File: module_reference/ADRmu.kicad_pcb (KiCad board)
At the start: 4 copper layers, 160 x 100 mm, 142 parts, among them J101 Harting 09042326831, J102 10Vf, J103 10Vs, J104 7Vref, J105 Lo, J301 Conn_01x01, J302 Conn_01x01, J303 Conn_01x01, J304 Conn_01x01, J305 Conn_01x01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

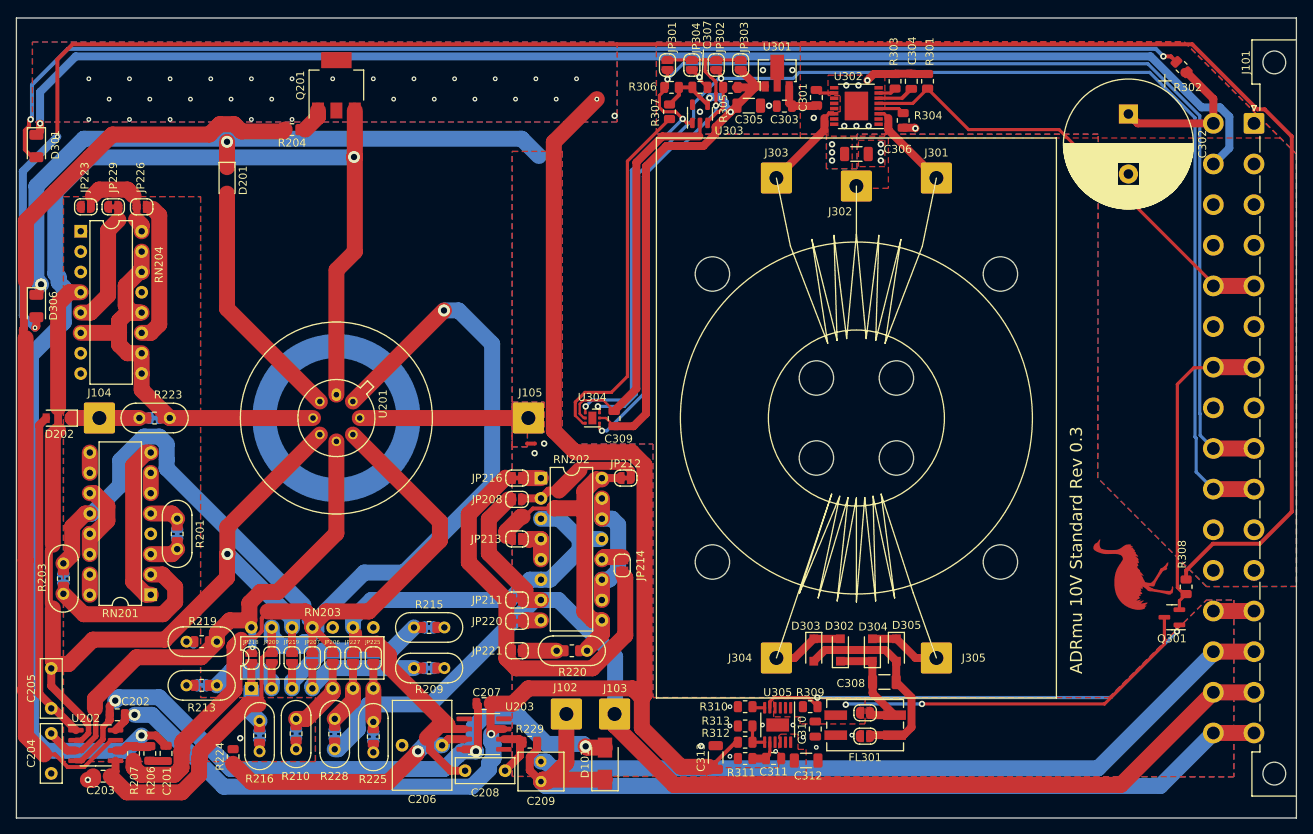
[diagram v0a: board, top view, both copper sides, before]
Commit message: switched to addressable eeprom
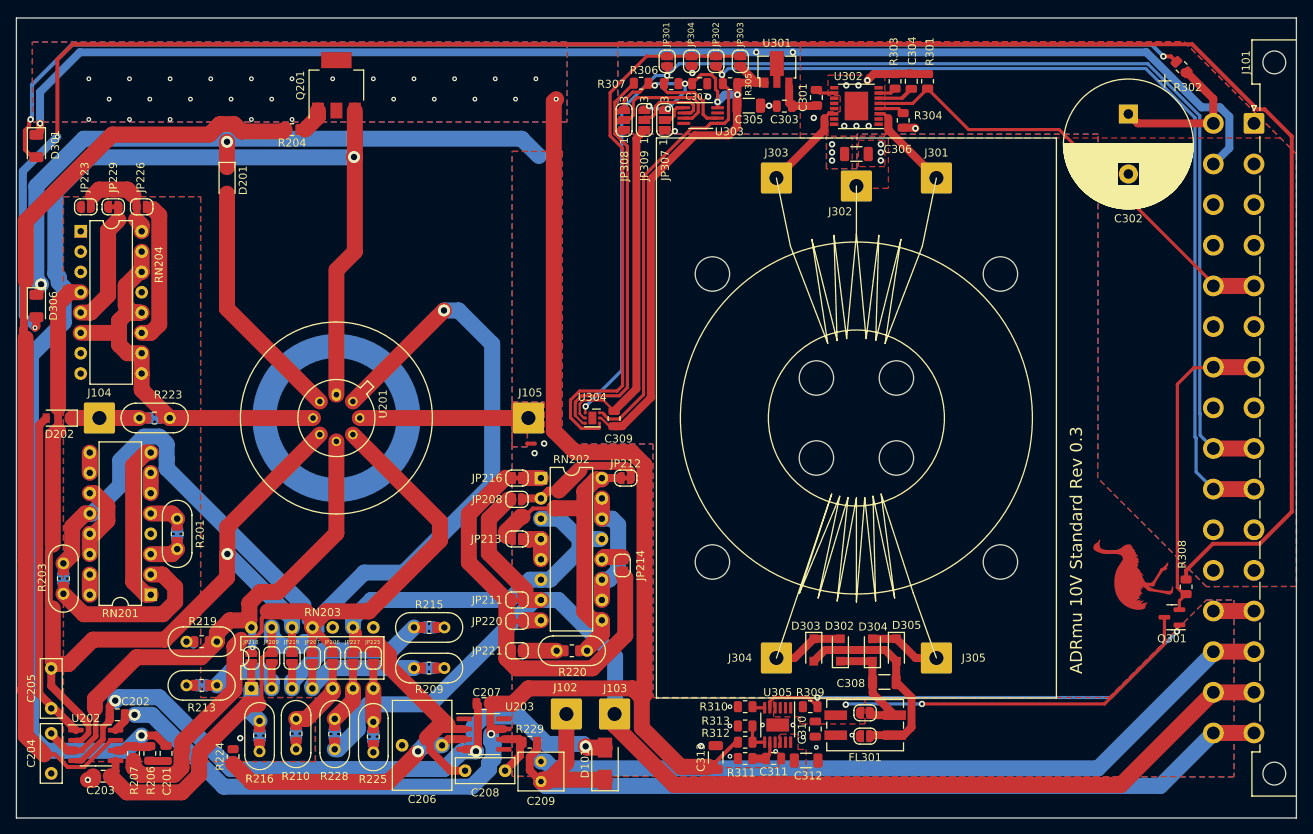
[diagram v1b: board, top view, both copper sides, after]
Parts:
- added JP307: Jumper_3_Open, Jumper:SolderJumper-3_P1.3mm_Open_RoundedPad1.0x1.5mm_NumberLabels, F.Cu at (151.0, 62.8)
- added JP308: Jumper_3_Open, Jumper:SolderJumper-3_P1.3mm_Open_RoundedPad1.0x1.5mm_NumberLabels, F.Cu at (146.0, 62.8)
- added JP309: Jumper_3_Open, Jumper:SolderJumper-3_P1.3mm_Open_RoundedPad1.0x1.5mm_NumberLabels, F.Cu at (148.5, 62.8)
- U303: value 24AA02-OT -> 24LC02; footprint Package_TO_SOT_SMD:SOT-23-5 -> Package_SO:MSOP-8_3x3mm_P0.65mm
- moved R307 5.03 mm to (148.1, 58.2), turned to 180 degrees
- moved JP301 0.47 mm to (151.3, 55.4)
- moved JP302 0.47 mm to (157.4, 55.4)
- moved JP303 0.47 mm to (160.5, 55.4)
- moved JP304 0.47 mm to (154.4, 55.4)
- moved C307 0.47 mm to (155.4, 58.2)
- moved R305 0.47 mm to (159.2, 58.2)
- moved R306 0.47 mm to (151.9, 58.2)
- moved U301 0.47 mm to (165.1, 56.4)
- moved U303 0.24 mm to (155.5, 62.2), turned to 0 degrees
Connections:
- U303 pad 1: /DC-DC/SCL -> /DC-DC/U303_a0
- U303 pad 2: GND -> /DC-DC/U303_a1
- U303 pad 3: /DC-DC/SDA -> /DC-DC/U303_a2
- U303 pad 4: +3V3 -> GND
- U303 pad 5: unconnected-(U303-Pad5) -> /DC-DC/SDA
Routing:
- net +3V3: track 73.4 -> 89.2 mm, vias 2 -> 6
- net /DC-DC/U303_a2: track 0.00 -> 15.0 mm
- net /DC-DC/U303_a1: track 0.00 -> 9.88 mm
- net GND: track 231.0 -> 224.0 mm, vias 16 -> 17
- net /DC-DC/U304_add0: track 64.0 -> 69.7 mm, vias 2 -> 0
- net /DC-DC/SCL: track 171.5 -> 176.7 mm, vias 3 -> 2
- net /DC-DC/U304_alert: track 45.5 -> 50.3 mm
- net /DC-DC/U303_a0: track 0.00 -> 3.40 mm
- net /DC-DC/SDA: track 172.3 -> 169.9 mm, vias 2 -> 1
- net /DC-DC/12Vf: track 188.0 -> 185.9 mm, vias 32 -> 29

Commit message: I shall waste not a copper
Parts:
- moved U304 3.35 mm to (144.5, 97.8)
- moved C309 3.35 mm to (147.2, 97.9)
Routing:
- net /DC-DC/U304_add0: track 69.7 -> 64.7 mm
- net /DC-DC/U304_alert: track 50.3 -> 45.3 mm
- net +3V3: track 89.2 -> 85.4 mm
- net /DC-DC/SDA: track 169.9 -> 166.4 mm
- net GNDA: track 177.8 -> 174.8 mm
- net /ref/ADR_Pin8: track 121.2 -> 118.6 mm
- net GND: track 224.0 -> 221.9 mm
- net /DC-DC/SCL: track 176.7 -> 174.6 mm
- net /ref/7Vref: track 13.3 -> 12.3 mm
- net /ref/U202B_out: track 116.1 -> 115.5 mm
- added copper zone on B.Cu, net /ref/10Vsense
- added copper zone on F.Cu, net /ref/ADR_Pin3
- added copper zone on B.Cu, net /ref/ADR_Pin4
- added copper zone on F.Cu, net /ref/ADR_Pin4
- added copper zone on F.Cu, net /ref/ADR_Pin6
- added copper zone on B.Cu, net /ref/ADR_Pin8
- added copper zone on F.Cu, net /ref/ADR_Pin8
- added copper zone on F.Cu, net /ref/RN202_Pin16
- added copper zone on F.Cu, net /ref/U203_-in
- added copper zone on B.Cu, net /ref/heater+
- added copper zone on F.Cu, net /ref/heater-

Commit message: asdf
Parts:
- moved D301 1.12 mm to (71.4, 66.0)
- moved D306 1.12 mm to (71.4, 86.0)
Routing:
- net /DC-DC/pwr_LED: track 155.8 -> 158.5 mm

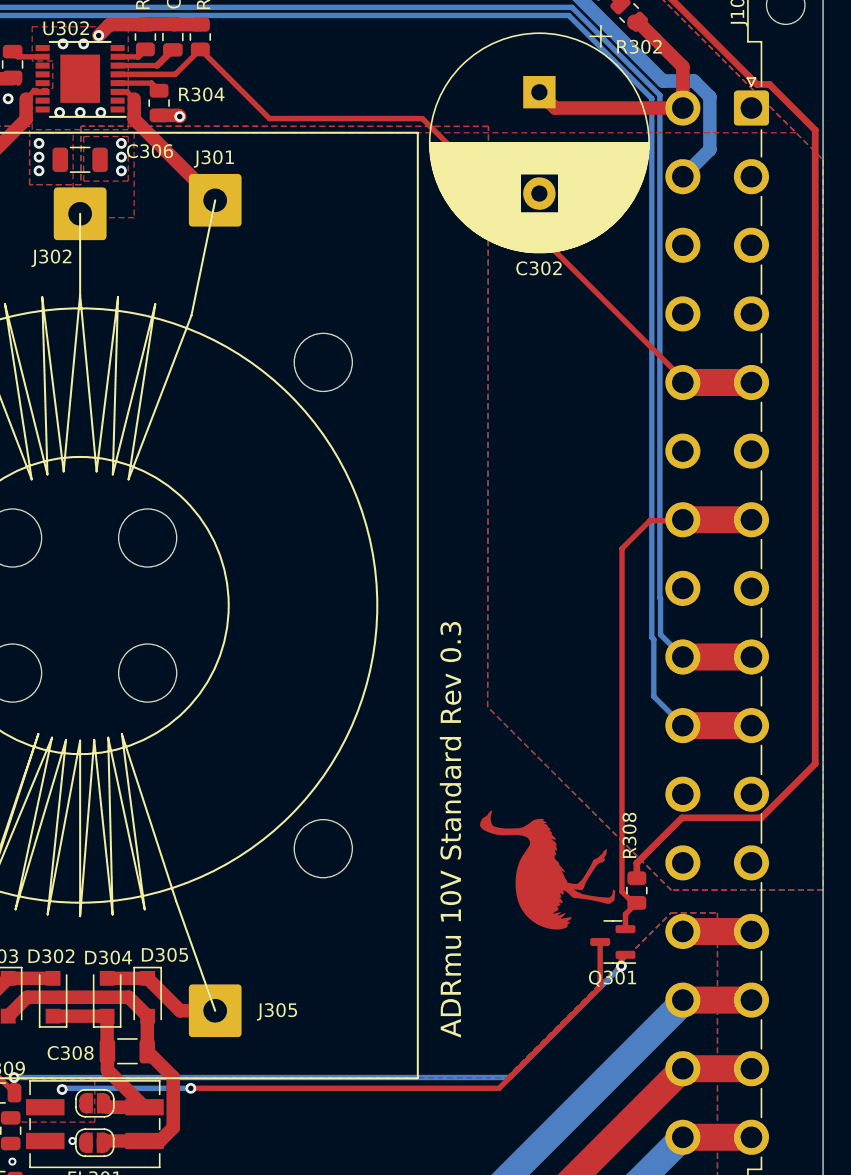
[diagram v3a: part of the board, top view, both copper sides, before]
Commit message: backplane connector changes
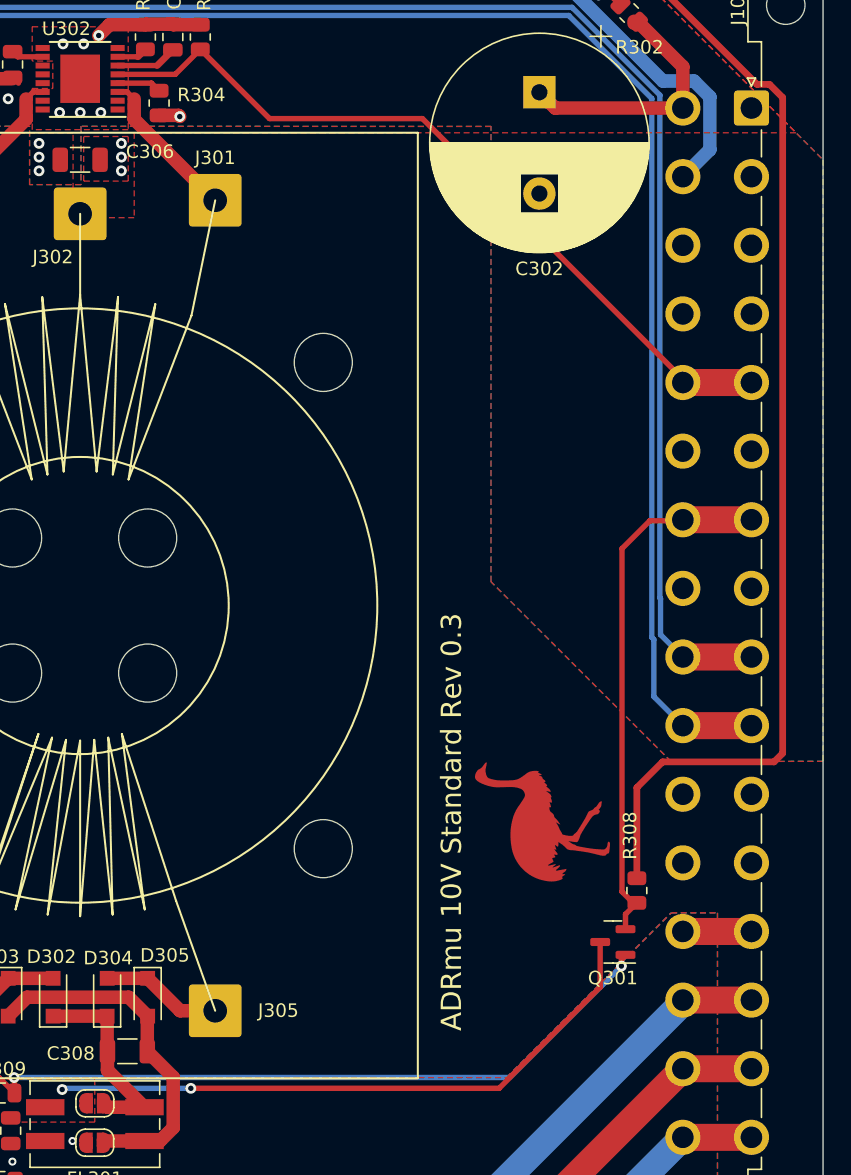
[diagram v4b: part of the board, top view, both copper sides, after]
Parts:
- moved SYM101 3.58 mm to (209.2, 116.0)
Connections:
- J101 pad a22: GND -> unconnected-(J101-Pada22)
- J101 pad a24: GND -> unconnected-(J101-Pada24)
- J101 pad c22: GND -> unconnected-(J101-Padc22)
- J101 pad c24: GND -> unconnected-(J101-Padc24)
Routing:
- net /DC-DC/status_LED: track 261.2 -> 260.6 mm
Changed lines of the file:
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@@
       (disableapertmacros false)
       (usegerberextensions false)
-      (usegerberattributes true)
+      (usegerberattributes false)
       (usegerberadvancedattributes true)
       (creategerberjobfile true)
@@
   (net 80 "/DC-DC/U303_a2")
   (net 81 "/DC-DC/U303_a1")
+  (net 82 "unconnected-(J101-Pada22)")
+  (net 83 "unconnected-(J101-Pada24)")
+  (net 84 "unconnected-(J101-Padc22)")
+  (net 85 "unconnected-(J101-Padc24)")
   (footprint "Resistor_SMD:R_0805_2012Metric" (layer "F.Cu")
     (at 151.8514 58.2096 180)
@@
       (net 6 "/DC-DC/SDA") (pinfunction "Pin_a20") (pintype "passive"))
     (pad "a22" thru_hole circle locked (at 53.34 0 270) (size 2.6 2.6) (drill 1.6) (layers *.Cu *.Mask)
-      (net 2 "GND") (pinfunction "Pin_a22") (pintype "passive"))
+      (net 82 "unconnected-(J101-Pada22)") (pinfunction "Pin_a22") (pintype "passive+no_connect"))
     (pad "a24" thru_hole circle locked (at 58.42 0 270) (size 2.6 2.6) (drill 1.6) (layers *.Cu *.Mask)
-      (net 2 "GND") (pinfunction "Pin_a24") (pintype "passive"))
+      (net 83 "unconnected-(J101-Pada24)") (pinfunction "Pin_a24") (pintype "passive+no_connect"))
     (pad "a26" thru_hole circle locked (at 63.5 0 270) (size 2.6 2.6) (drill 1.6) (layers *.Cu *.Mask)
       (net 76 "GNDA") (pinfunction "Pin_a26") (pintype "passive"))
@@
       (net 6 "/DC-DC/SDA") (pinfunction "Pin_c20") (pintype "passive"))
     (pad "c22" thru_hole circle locked (at 53.34 5.08 270) (size 2.6 2.6) (drill 1.6) (layers *.Cu *.Mask)
-      (net 2 "GND") (pinfunction "Pin_c22") (pintype "passive"))
+      (net 84 "unconnected-(J101-Padc22)") (pinfunction "Pin_c22") (pintype "passive+no_connect"))
     (pad "c24" thru_hole circle locked (at 58.42 5.08 270) (size 2.6 2.6) (drill 1.6) (layers *.Cu *.Mask)
-      (net 2 "GND") (pinfunction "Pin_c24") (pintype "passive"))
+      (net 85 "unconnected-(J101-Padc24)") (pinfunction "Pin_c24") (pintype "passive+no_connect"))
     (pad "c26" thru_hole circle locked (at 63.5 5.08 270) (size 2.6 2.6) (drill 1.6) (layers *.Cu *.Mask)
       (net 76 "GNDA") (pinfunction "Pin_c26") (pintype "passive"))
@@
     (fp_line (start -1.95 2.45) (end -1.95 -1.475) (layer "F.Fab") (width 0.1))
     (pad "1" smd roundrect locked (at -2.475 -1.905) (size 1.95 0.6) (layers "F.Cu" "F.Paste" "F.Mask") (roundrect_rratio 0.25)
-      (net 7 "unconnected-(U203-Pad1)") (pinfunction "~{PD}") (pintype "input"))
+      (net 7 "unconnected-(U203-Pad1)") (pinfunction "~{PD}") (pintype "input+no_connect"))
     (pad "2" smd roundrect locked (at -2.475 -0.635) (size 1.95 0.6) (layers "F.Cu" "F.Paste" "F.Mask") (roundrect_rratio 0.25)
       (net 35 "/ref/U203_-in") (pinfunction "-") (pintype "input"))
@@
       (net 24 "/DC-DC/12Vf") (pinfunction "V+") (pintype "power_in"))
     (pad "8" smd roundrect locked (at 2.475 -1.905) (size 1.95 0.6) (layers "F.Cu" "F.Paste" "F.Mask") (roundrect_rratio 0.25)
-      (net 8 "unconnected-(U203-Pad8)") (pinfunction "SDCOM") (pintype "passive"))
+      (net 8 "unconnected-(U203-Pad8)") (pinfunction "SDCOM") (pintype "passive+no_connect"))
     (model "${KICAD6_3DMODEL_DIR}/Package_SO.3dshapes/SOIC-8_3.9x4.9mm_P1.27mm.wrl"
       (offset (xyz 0 0 0))
@@
   )
   (footprint "ADRmu_Library:osmu_logo" (layer "F.Cu")
-    (at 209.611 119.576 90)
+    (at 209.23 116.02 90)
     (property "Sheetfile" "ADRmu.kicad_sch")
     (property "Sheetname" "")
@@
   (gr_line (start 230 147) (end 70 147) (layer "Dwgs.User") (width 0.15))
   (gr_rect (start 230 50) (end 70 150) (layer "Edge.Cuts") (width 0.1) (fill none))
-  (gr_text "ADRmu 10V Standard Rev 0.3" (at 202.499 116.528 90) (layer "F.SilkS")
+  (gr_text "ADRmu 10V Standard Rev 0.3" (at 202.499 116.02 90) (layer "F.SilkS")
     (effects (font (size 1.5 1.5) (thickness 0.3)))
   )
@@
   (segment (start 185 130) (end 182.4 130) (width 1) (layer "F.Cu") (net 32))
   (segment (start 177 127.6) (end 180 127.6) (width 1) (layer "F.Cu") (net 32))
+  (segment (start 218.12 111.575) (end 226.375 111.575) (width 0.5) (layer "F.Cu") (net 33))
+  (segment (start 226.375 111.575) (end 227.01 110.94) (width 0.5) (layer "F.Cu") (net 33))
   (segment (start 71.375 88.8) (end 71.375 87.4) (width 1) (layer "F.Cu") (net 33))
-  (segment (start 75.118 55.187) (end 75.118 64.839) (width 0.5) (layer "F.Cu") (net 33))
-  (segment (start 77.023 53.282) (end 75.118 55.187) (width 0.5) (layer "F.Cu") (net 33))
-  (segment (start 216.977 53.282) (end 77.023 53.282) (width 0.5) (layer "F.Cu") (net 33))
-  (segment (start 219.563489 115.719511) (end 225.424672 115.719511) (width 0.5) (layer "F.Cu") (net 33))
-  (segment (start 229.423 64.80373) (end 226.03975 61.42048) (width 0.5) (layer "F.Cu") (net 33))
   (segment (start 225.11548 61.42048) (end 216.977 53.282) (width 0.5) (layer "F.Cu") (net 33))
-  (segment (start 216.215 119.068) (end 219.563489 115.719511) (width 0.5) (layer "F.Cu") (net 33))
-  (segment (start 225.424672 115.719511) (end 229.423 111.721183) (width 0.5) (layer "F.Cu") (net 33))
+  (segment (start 216.977 53.282) (end 77.023 53.282) (width 0.5) (layer "F.Cu") (net 33))
+  (segment (start 216.215 113.48) (end 218.12 111.575) (width 0.5) (layer "F.Cu") (net 33))
+  (segment (start 77.023 53.282) (end 75.118 55.187) (width 0.5) (layer "F.Cu") (net 33))
+  (segment (start 227.01 62.39073) (end 226.03975 61.42048) (width 0.5) (layer "F.Cu") (net 33))
   (segment (start 226.03975 61.42048) (end 225.11548 61.42048) (width 0.5) (layer "F.Cu") (net 33))
-  (segment (start 229.423 111.721183) (end 229.423 64.80373) (width 0.5) (layer "F.Cu") (net 33))
-  (segment (start 216.215 120.1875) (end 216.215 119.068) (width 0.5) (layer "F.Cu") (net 33))
+  (segment (start 227.01 110.94) (end 227.01 62.39073) (width 0.5) (layer "F.Cu") (net 33))
+  (segment (start 75.118 55.187) (end 75.118 64.839) (width 0.5) (layer "F.Cu") (net 33))
+  (segment (start 216.215 120.1875) (end 216.215 113.48) (width 0.5) (layer "F.Cu") (net 33))
   (via (at 71.375 88.8) (size 0.6) (drill 0.3) (layers "F.Cu" "B.Cu") (net 33))
   (via (at 75.118 64.839) (size 0.6) (drill 0.3) (layers "F.Cu" "B.Cu") (net 33))
@@
       (pts
         (xy 230 67)
-        (xy 230.007474 121.05838)
-        (xy 218.762474 121.073523)
-        (xy 205.166 107.511)
-        (xy 205.231954 64.530143)
+        (xy 229.994647 111.533395)
+        (xy 218.749647 111.548538)
+        (xy 205.42 98.24)
+        (xy 205.42 64.530143)
         (xy 175.066983 64.521807)
         (xy 175.066891 68.839737)

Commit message: asdf
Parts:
- moved SYM101 3.81 mm to (209.2, 112.2)
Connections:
- J101 pad a16: GND -> /DC-DC/SCL
- J101 pad a18: /DC-DC/SCL -> /DC-DC/SDA
- J101 pad a20: /DC-DC/SDA -> unconnected-(J101-Pada20)
- J101 pad a6: GND -> unconnected-(J101-Pada6)
- J101 pad a8: GND -> unconnected-(J101-Pada8)
- J101 pad c16: GND -> /DC-DC/SCL
- J101 pad c18: /DC-DC/SCL -> /DC-DC/SDA
- J101 pad c20: /DC-DC/SDA -> unconnected-(J101-Padc20)
- J101 pad c6: GND -> unconnected-(J101-Padc6)
- J101 pad c8: GND -> unconnected-(J101-Padc8)
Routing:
- net /DC-DC/SDA: track 166.4 -> 161.3 mm
- net /DC-DC/SCL: track 174.6 -> 169.5 mm
- net /DC-DC/status_LED: track 260.6 -> 259.9 mm
